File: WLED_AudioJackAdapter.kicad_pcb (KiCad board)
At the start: 2 copper layers, 28.6 x 12.7 mm, 8 parts, among them J1 AudioJack4, J2 Conn_01x03_Female

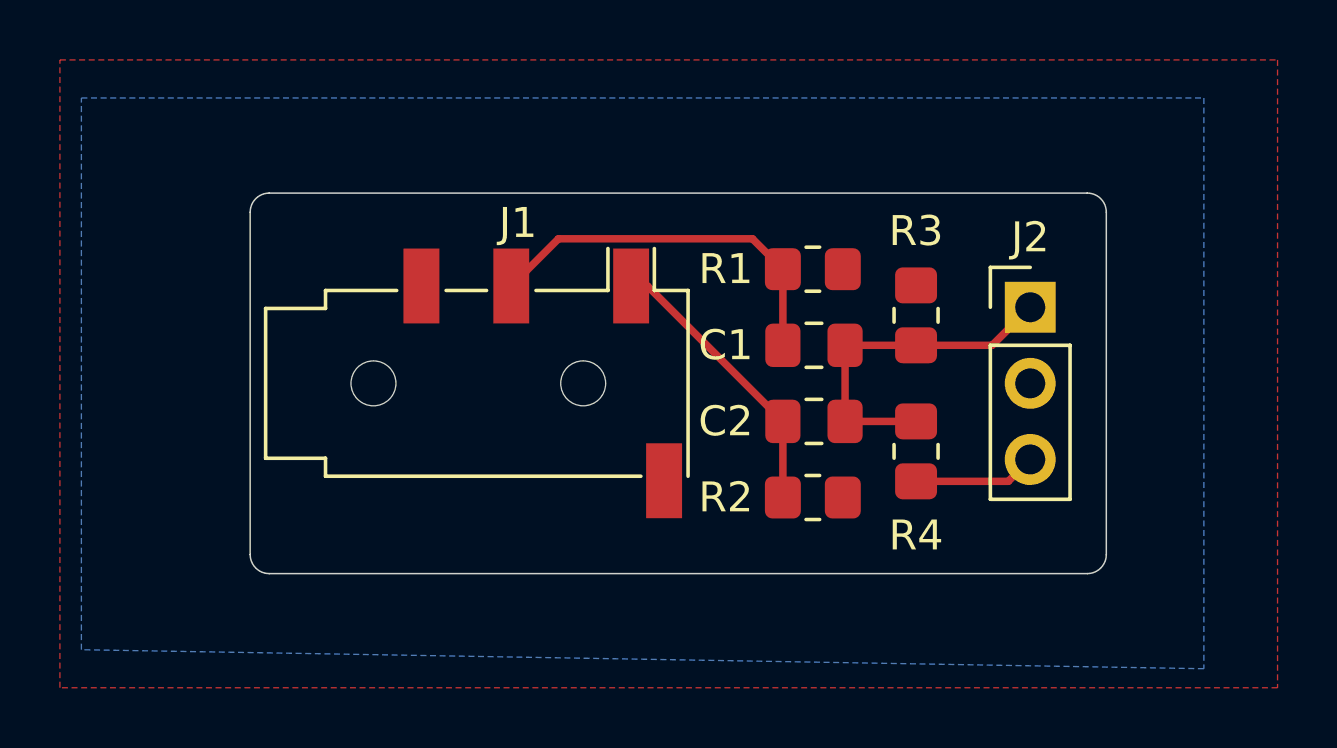
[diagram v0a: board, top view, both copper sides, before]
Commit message: - update to kicad 6
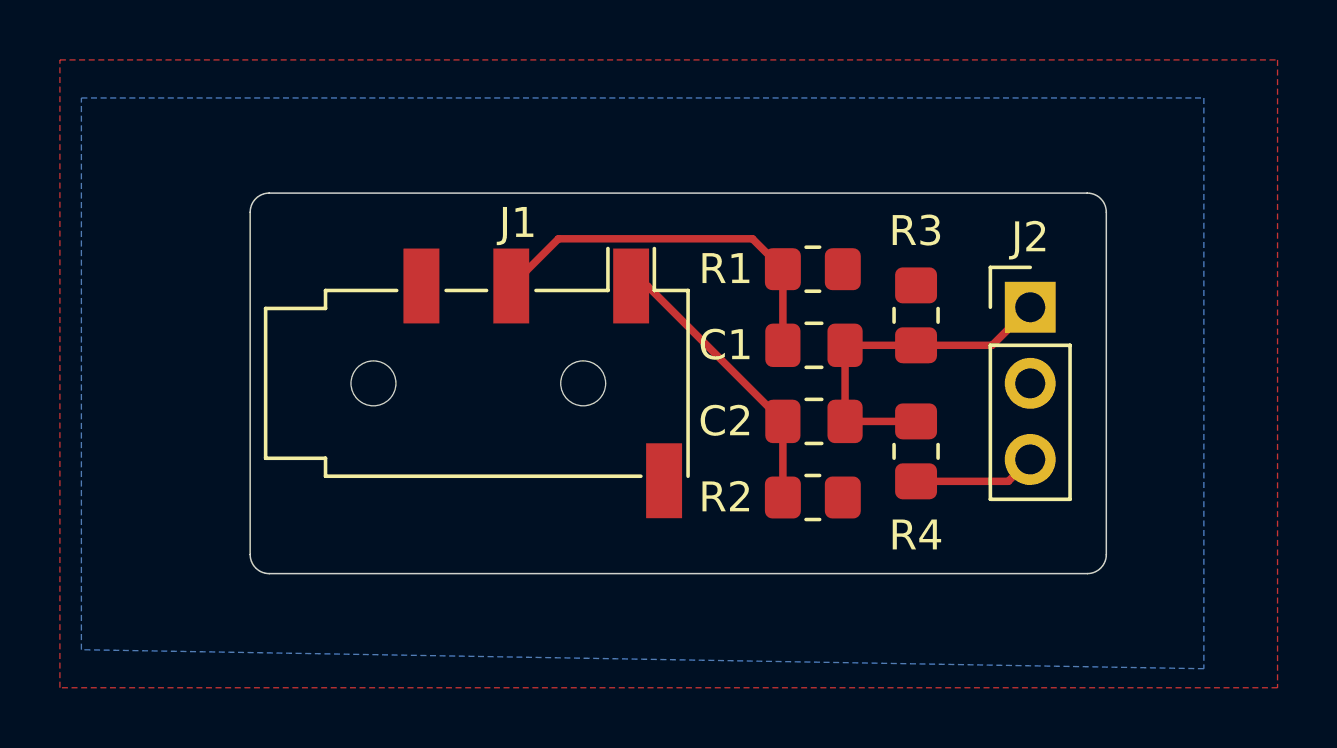
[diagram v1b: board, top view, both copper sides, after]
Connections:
- J1 pad R2: (no net) -> unconnected-(J1-PadR2)
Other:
- net class Default removed
